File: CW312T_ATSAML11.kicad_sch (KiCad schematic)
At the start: 16 parts, among them P1 PCIEx4 EDGE CONNECTOR, U1 ATSMAL11E16A-AU

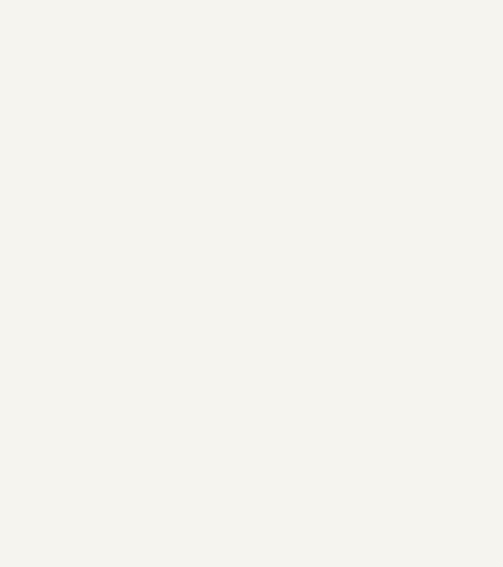
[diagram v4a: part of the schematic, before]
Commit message: updated silkscreen symbols
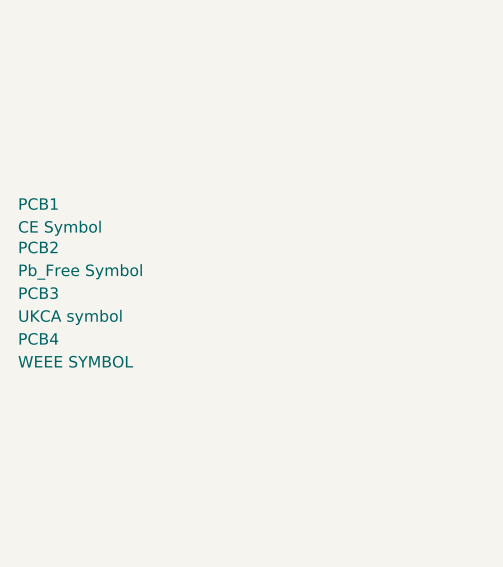
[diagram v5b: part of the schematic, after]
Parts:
- removed PCB3: WEEE, Silkscrren_Symbols:WEEE-Logo_5.6x8mm_SilkScreen, symbol Silkscreen_Symbols:WEEE
- removed PCB4: UKCA symbol, Silkscrren_Symbols:UKCA-Logo_8x8mm_SilkScreen, symbol Silkscreen_Symbols:UKCA
- added PCB3: UKCA symbol, Silkscrren_Symbols:UKCA-Logo_8x8mm_SilkScreen, symbol Silkscreen_Symbols:UKCA
- added PCB4: WEEE SYMBOL, Silkscrren_Symbols:WEEE-Logo_5.6x8mm_SilkScreen, symbol Silkscreen_Symbols:WEEE
- PCB1: value CE -> CE Symbol
- PCB2: value Pb_Free -> Pb_Free Symbol
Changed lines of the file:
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@@
-	)
-	(symbol
-		(lib_id "Silkscreen_Symbols:Pb_Free")
-		(at -19.05 198.12 0)
-		(unit 1)
-		(exclude_from_sim no)
-		(in_bom no)
-		(on_board yes)
-		(dnp no)
-		(fields_autoplaced yes)
-		(property "Reference" "PCB2"
-			(at -19.05 198.12 0)
-			(effects
-				(font
-					(size 1.27 1.27)
-				)
-				(hide yes)
-			)
-		)
-		(property "Value" "Pb_Free"
-			(at -19.05 198.12 0)
-			(effects
-				(font
-					(size 1.27 1.27)
-				)
-				(hide yes)
-			)
-		)
-		(property "Footprint" "Silkscrren_Symbols:Pb_Free_8.0x8.0mm_SilkScreen"
-			(at -19.05 198.12 0)
-			(effects
-				(font
-					(size 1.27 1.27)
-				)
-				(hide yes)
-			)
-		)
-		(property "Datasheet" ""
-			(at -19.05 198.12 0)
-			(effects
-				(font
-					(size 1.27 1.27)
-				)
-				(hide yes)
-			)
-		)
-		(property "Description" ""
-			(at -19.05 198.12 0)
-			(effects
-				(font
-					(size 1.27 1.27)
-				)
-				(hide yes)
-			)
-		)
-		(instances
-			(project ""
-				(path "/497ddeb2-6500-4436-ac31-e3cfdb79cc3f"
-					(reference "PCB2")
-					(unit 1)
-				)
-			)
-		)
 	)
 	(symbol
@@
 	)
 	(symbol
-		(lib_id "Silkscreen_Symbols:UKCA")
-		(at -16.51 193.04 0)
-		(unit 1)
-		(exclude_from_sim no)
-		(in_bom yes)
-		(on_board yes)
-		(dnp no)
-		(fields_autoplaced yes)
-		(property "Reference" "PCB4"
-			(at -13.97 191.7699 0)
-			(effects
-				(font
-					(size 1.27 1.27)
-				)
-				(justify left)
-				(hide yes)
-			)
-		)
-		(property "Value" "UKCA symbol"
-			(at -13.97 193.0399 0)
-			(effects
-				(font
-					(size 1.27 1.27)
-				)
-				(justify left)
-				(hide yes)
-			)
-		)
-		(property "Footprint" "Silkscrren_Symbols:UKCA-Logo_8x8mm_SilkScreen"
-			(at -16.51 193.04 0)
-			(effects
-				(font
-					(size 1.27 1.27)
-				)
-				(hide yes)
-			)
-		)
-		(property "Datasheet" ""
-			(at -16.51 193.04 0)
-			(effects
-				(font
-					(size 1.27 1.27)
-				)
-				(hide yes)
-			)
-		)
-		(property "Description" ""
-			(at -16.51 193.04 0)
-			(effects
-				(font
-					(size 1.27 1.27)
-				)
-				(hide yes)
-			)
-		)
-		(instances
-			(project ""
-				(path "/497ddeb2-6500-4436-ac31-e3cfdb79cc3f"
-					(reference "PCB4")
-					(unit 1)
-				)
-			)
-		)
-	)
-	(symbol
 		(lib_id "power:GND")
 		(at 189.23 53.34 0)
@@
 	)
 	(symbol
+		(lib_id "Silkscreen_Symbols:UKCA")
+		(at -36.83 171.45 0)
+		(unit 1)
+		(exclude_from_sim no)
+		(in_bom yes)
+		(on_board yes)
+		(dnp no)
+		(fields_autoplaced yes)
+		(property "Reference" "PCB3"
+			(at -34.29 170.1799 0)
+			(effects
+				(font
+					(size 1.27 1.27)
+				)
+				(justify left)
+			)
+		)
+		(property "Value" "UKCA symbol"
+			(at -34.29 172.7199 0)
+			(effects
+				(font
+					(size 1.27 1.27)
+				)
+				(justify left)
+			)
+		)
+		(property "Footprint" "Silkscrren_Symbols:UKCA-Logo_8x8mm_SilkScreen"
+			(at -36.83 171.45 0)
+			(effects
+				(font
+					(size 1.27 1.27)
+				)
+				(hide yes)
+			)
+		)
+		(property "Datasheet" ""
+			(at -36.83 171.45 0)
+			(effects
+				(font
+					(size 1.27 1.27)
+				)
+				(hide yes)
+			)
+		)
+		(property "Description" ""
+			(at -36.83 171.45 0)
+			(effects
+				(font
+					(size 1.27 1.27)
+				)
+				(hide yes)
+			)
+		)
+		(instances
+			(project ""
+				(path "/497ddeb2-6500-4436-ac31-e3cfdb79cc3f"
+					(reference "PCB3")
+					(unit 1)
+				)
+			)
+		)
+	)
+	(symbol
 		(lib_id "power:+3V3")
 		(at 74.93 76.2 0)
@@
 	)
 	(symbol
-		(lib_id "Silkscreen_Symbols:CE_Free")
-		(at -25.4 199.39 0)
+		(lib_id "Silkscreen_Symbols:Pb_Free")
+		(at -36.83 166.37 0)
 		(unit 1)
 		(exclude_from_sim no)
@@
 		(dnp no)
 		(fields_autoplaced yes)
-		(property "Reference" "PCB1"
-			(at -27.94 193.04 0)
-			(effects
-				(font
-					(size 1.27 1.27)
-				)
-				(hide yes)
-			)
-		)
-		(property "Value" "CE"
-			(at -25.4 199.39 0)
-			(effects
-				(font
-					(size 1.27 1.27)
-				)
-				(hide yes)
-			)
-		)
-		(property "Footprint" "Silkscrren_Symbols:CE-Logo_8.5x6mm_SilkScreen"
-			(at -25.4 199.39 0)
+		(property "Reference" "PCB2"
+			(at -34.29 165.0999 0)
+			(effects
+				(font
+					(size 1.27 1.27)
+				)
+				(justify left)
+			)
+		)
+		(property "Value" "Pb_Free Symbol"
+			(at -34.29 167.6399 0)
+			(effects
+				(font
+					(size 1.27 1.27)
+				)
+				(justify left)
+			)
+		)
+		(property "Footprint" "Silkscrren_Symbols:Pb_Free_8.0x8.0mm_SilkScreen"
+			(at -36.83 166.37 0)
 			(effects
 				(font
@@
 		)
 		(property "Datasheet" ""
-			(at -25.4 199.39 0)
+			(at -36.83 166.37 0)
 			(effects
 				(font
@@
 		)
 		(property "Description" ""
-			(at -25.4 199.39 0)
+			(at -36.83 166.37 0)
 			(effects
 				(font
@@
 			(project ""
 				(path "/497ddeb2-6500-4436-ac31-e3cfdb79cc3f"
-					(reference "PCB1")
+					(reference "PCB2")
 					(unit 1)
 				)
@@
 	)
 	(symbol
-		(lib_id "Silkscreen_Symbols:WEEE")
-		(at -19.05 196.85 0)
-		(unit 1)
-		(exclude_from_sim no)
-		(in_bom no)
-		(on_board yes)
-		(dnp no)
-		(fields_autoplaced yes)
-		(property "Reference" "PCB3"
-			(at -20.32 192.405 0)
-			(effects
-				(font
-					(size 1.27 1.27)
-				)
-				(hide yes)
-			)
-		)
-		(property "Value" "WEEE"
-			(at -19.05 196.85 0)
-			(effects
-				(font
-					(size 1.27 1.27)
-				)
-				(hide yes)
-			)
-		)
-		(property "Footprint" "Silkscrren_Symbols:WEEE-Logo_5.6x8mm_SilkScreen"
-			(at -19.05 196.85 0)
-			(effects
-				(font
-					(size 1.27 1.27)
-				)
-				(hide yes)
-			)
-		)
-		(property "Datasheet" ""
-			(at -19.05 196.85 0)
-			(effects
-				(font
-					(size 1.27 1.27)
-				)
-				(hide yes)
-			)
-		)
-		(property "Description" ""
-			(at -19.05 196.85 0)
-			(effects
-				(font
-					(size 1.27 1.27)
-				)
-				(hide yes)
-			)
-		)
-		(instances
-			(project ""
-				(path "/497ddeb2-6500-4436-ac31-e3cfdb79cc3f"
-					(reference "PCB3")
-					(unit 1)
-				)
-			)
-		)
-	)
-	(symbol
 		(lib_id "tutorial_2_library:CAP_2u2_16V_0603")
 		(at 44.45 35.56 270)
@@
 					(unit 1)
 				)
+			)
+		)
+	)
+	(symbol
+		(lib_id "Silkscreen_Symbols:CE_Free")
+		(at -36.83 160.02 0)
+		(unit 1)
+		(exclude_from_sim no)
+		(in_bom no)
+		(on_board yes)
+		(dnp no)
+		(property "Reference" "PCB1"
+			(at -34.29 160.274 0)
+			(effects
+				(font
+					(size 1.27 1.27)
+				)
+				(justify left)
+			)
+		)
+		(property "Value" "CE Symbol"
+			(at -34.29 162.814 0)
+			(effects
+				(font
+					(size 1.27 1.27)
+				)
+				(justify left)
+			)
+		)
+		(property "Footprint" "Silkscrren_Symbols:CE-Logo_8.5x6mm_SilkScreen"
+			(at -36.83 160.02 0)
+			(effects
+				(font
+					(size 1.27 1.27)
+				)
+				(hide yes)
+			)
+		)
+		(property "Datasheet" ""
+			(at -36.83 160.02 0)
+			(effects
+				(font
+					(size 1.27 1.27)
+				)
+				(hide yes)
+			)
+		)
+		(property "Description" ""
+			(at -36.83 160.02 0)
+			(effects
+				(font
+					(size 1.27 1.27)
+				)
+				(hide yes)
+			)
+		)
+		(instances
+			(project ""
+				(path "/497ddeb2-6500-4436-ac31-e3cfdb79cc3f"
+					(reference "PCB1")
+					(unit 1)
+				)
+			)
+		)
+	)
+	(symbol
+		(lib_id "Silkscreen_Symbols:WEEE")
+		(at -36.83 176.53 0)
+		(unit 1)
+		(exclude_from_sim no)
+		(in_bom no)
+		(on_board yes)
+		(dnp no)
+		(fields_autoplaced yes)
+		(property "Reference" "PCB4"
+			(at -34.29 175.2599 0)
+			(effects
+				(font
+					(size 1.27 1.27)
+				)
+				(justify left)
+			)
+		)
+		(property "Value" "WEEE SYMBOL"
+			(at -34.29 177.7999 0)
+			(effects
+				(font
+					(size 1.27 1.27)
+				)
+				(justify left)
+			)
+		)
+		(property "Footprint" "Silkscrren_Symbols:WEEE-Logo_5.6x8mm_SilkScreen"
+			(at -36.83 176.53 0)
+			(effects
+				(font
+					(size 1.27 1.27)
+				)
+				(hide yes)
+			)
+		)
+		(property "Datasheet" ""
+			(at -36.83 176.53 0)
+			(effects
+				(font
+					(size 1.27 1.27)
+				)
+				(hide yes)
+			)
+		)
+		(property "Description" ""
+			(at -36.83 176.53 0)
+			(effects
+				(font
+					(size 1.27 1.27)
+				)
+				(hide yes)
+			)
+		)
+		(instances
+			(project ""
+				(path "/497ddeb2-6500-4436-ac31-e3cfdb79cc3f"
+					(reference "PCB4")
+					(unit 1)
+				)

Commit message: updated schematic and pcb after library re-organization
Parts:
- removed P1: PCIEx4 EDGE CONNECTOR, tutorial_2_library:CW312_Template, symbol tutorial_2_library:CW312T-Template
- removed U1: ATSMAL11E16A-AU, Package_QFP:TQFP-32_7x7mm_P0.8mm, symbol tutorial_2_library:ATSMAL11E16A-AU
- added P1: PCIEx4 EDGE CONNECTOR, tutorial_2_library:CW312_Template, symbol Connectors:CW312T-Template
- added U1: ATSMAL11E16A-AU, Package_QFP:TQFP-32_7x7mm_P0.8mm, symbol Integrated_Circuits:ATSMAL11E16A-AU
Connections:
- net +1V2: now also P1.B5 (FILTIN), P1.B7 (VCC1.2)
- net +3V3: now also P1.A26 (JTAG_VREF), P1.A5 (VCC3.3), P1.B10 (IOVREF), U1.30 (VDDIO), U1.9 (VDDANA)
- net ENTRY: now also P1.B25 (CW_PDIC), U1.20 (PA19)
- net GND: now also P1.A1 (GND), P1.A2 (GND), P1.A20 (GND), P1.A27 (GND), P1.A28 (GND), P1.A8 (GND), P1.B15 (GND), P1.B21 (GND), P1.B22 (GND), P1.B3 (GND), P1.B9 (GND), U1.10 (GNDANA), U1.28 (GND)
- net GPIO3: now also P1.B18 (GPIO3), U1.19 (PA18)
- net GPIO4: now also P1.B19 (GPIO4), U1.21 (PA22)
- net LED1: now also P1.B11 (LED1), U1.24 (PA25)
- net LED2: now also P1.B12 (LED2), U1.23 (PA24)
- net LED3: now also P1.B13 (LED3), U1.22 (PA23)
- net RST: now also P1.A31 (JTAG_nRST), P1.B14 (nRST)
- net RX: now also P1.B17 (GPIO2/RX), U1.18 (PA17)
- net SHUNTH: now also P1.A3 (FILT_LP), P1.B2 (SHUNTH), P1.B4 (FILT_HP)
- net SWCLK: now also P1.B32 (JTAG_TCK), U1.31 (PA30/SWCLK)
- net SWDIO: now also P1.B31 (JTAG_TMS), U1.32 (PA31/SWDIO)
- net TX: now also P1.B16 (GPIO1/TX), U1.17 (PA16)
- net VDDCORE: now also P1.B1 (SHUNTL), U1.27 (VDDCORE)
- net XIN: now also U1.15 (PA14/XOSC)
- net at C7.1, R3.1: now also U1.26 (~{RESET})
- net at R2.1: now also P1.B27 (CLKOUT)
